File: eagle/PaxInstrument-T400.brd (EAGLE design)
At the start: 96.5 x 50.8 mm, 121 parts, among them IC1 MCP3424, U1 MCP9800, U3 MCP73831, U4 MIC5219-3.3V, U7 USD-SOCKETNEW, U8 NC7S32, X2 FH12-12S-0.5SH, Y1 RESONATORSMD

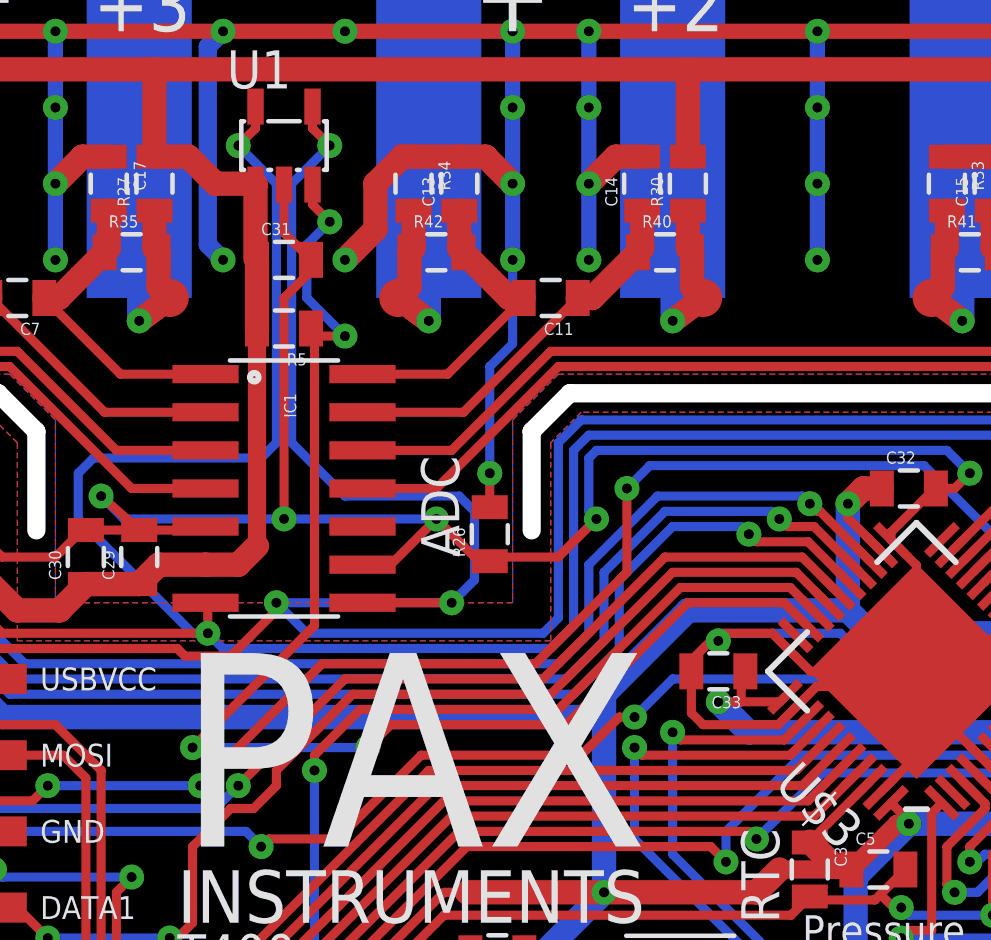
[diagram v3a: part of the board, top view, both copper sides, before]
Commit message: - Removed TEMP_INT
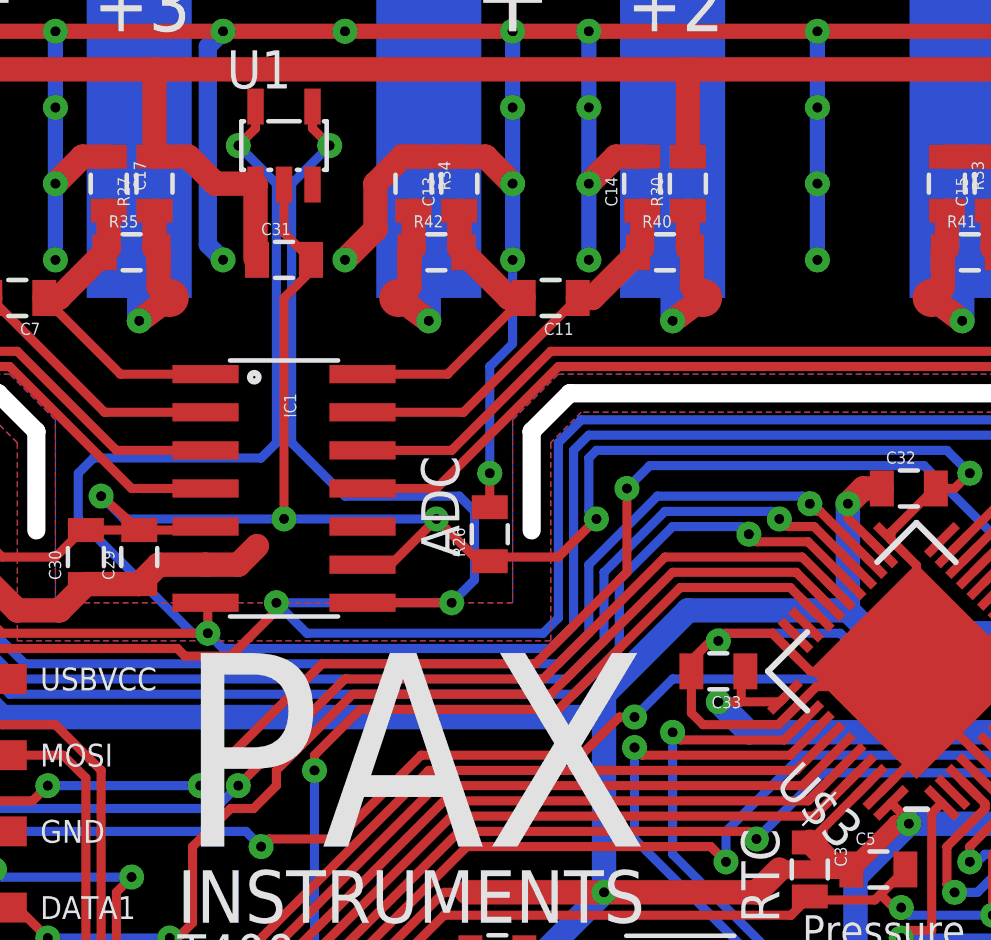
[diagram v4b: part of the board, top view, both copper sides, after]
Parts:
- removed R5: 10k, SparkFun-Passives:0805
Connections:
- removed net TEMP_INT: R5.1, U$3.31, U1.3
- new net DATA3: U$3.31
- net 3.3V: no longer R5.2
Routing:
- net TEMP_INT: track 45.8 -> 0.00 mm, vias 4 -> 0
- net 3.3V: track 365.2 -> 355.7 mm
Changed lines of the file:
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@@
 <attribute name="OC_DIGIKEY" value="N/A" x="57.15" y="44.45" size="1.778" layer="28" rot="MR180" display="off"/>
-</element>
-<element name="R5" library="SparkFun-Passives" package="0805" value="10k" x="48.26" y="38.354" rot="R180">
-<attribute name="OC_DIGIKEY" value="1276-5086-2-ND" x="48.26" y="38.354" size="1.778" layer="27" font="vector" ratio="15" rot="R180" display="off"/>
 </element>
 <element name="Z1" library="freetronics-master-v1.1" package="0603" value="PGB1010603" x="90.17" y="29.972" rot="R180">
@@
 <contactref element="U$3" pad="14"/>
 <contactref element="U$3" pad="34"/>
-<contactref element="R5" pad="2"/>
 <contactref element="U$14" pad="2"/>
 <contactref element="R16" pad="1"/>
@@
 <wire x1="45.6438" y1="30.48" x2="46.736" y2="30.48" width="0.8128" layer="1"/>
 <wire x1="46.736" y1="30.48" x2="47.36" y2="31.104" width="0.8128" layer="1"/>
-<wire x1="47.36" y1="31.104" x2="47.36" y2="38.354" width="0.6096" layer="1"/>
-<wire x1="47.36" y1="38.354" x2="47.36" y2="40.64" width="0.8128" layer="1"/>
 <wire x1="47.36" y1="40.64" x2="47.31" y2="40.69" width="0.6096" layer="1"/>
 <wire x1="47.31" y1="40.69" x2="47.31" y2="43.15" width="0.8128" layer="1"/>
@@
 <wire x1="28.702" y1="31.242" x2="29.464" y2="30.48" width="0.8128" layer="1"/>
 <contactref element="X2" pad="1"/>
-<wire x1="49.01" y1="12.61" x2="45.51" y2="12.61" width="0" layer="19" extent="1-1"/>
+<wire x1="47.36" y1="31.104" x2="47.36" y2="40.64" width="0" layer="19" extent="1-1"/>
+<wire x1="45.51" y1="12.61" x2="49.01" y2="12.61" width="0" layer="19" extent="1-1"/>
 </signal>
 <signal name="3V3EN">
@@
 <wire x1="49.276" y1="24.13" x2="49.276" y2="23.622" width="0.3048" layer="1"/>
 </signal>
-<signal name="TEMP_INT">
-<contactref element="U1" pad="3"/>
-<contactref element="R5" pad="1"/>
-<contactref element="U$3" pad="31"/>
-<wire x1="65.66504375" y1="28.479634375" x2="64.934678125" y2="29.21" width="0.3048" layer="1"/>
-<wire x1="64.934678125" y1="29.21" x2="61.722" y2="29.21" width="0.3048" layer="1"/>
-<wire x1="61.722" y1="29.21" x2="57.658" y2="25.146" width="0.3048" layer="1"/>
-<wire x1="57.658" y1="25.146" x2="51.816" y2="25.146" width="0.3048" layer="1"/>
-<wire x1="49.276" y1="28.448" x2="49.276" y2="37.962" width="0.3048" layer="1"/>
-<wire x1="49.276" y1="37.962" x2="49.16" y2="38.354" width="0.3048" layer="1"/>
-<wire x1="49.21" y1="43.15" x2="49.21" y2="42.484" width="0.3048" layer="1"/>
-<wire x1="49.21" y1="42.484" x2="49.784" y2="41.91" width="0.3048" layer="1"/>
-<via x="49.784" y="41.91" extent="1-16" drill="0.3302"/>
-<wire x1="49.784" y1="41.91" x2="49.022" y2="41.148" width="0.3048" layer="16"/>
-<wire x1="49.022" y1="41.148" x2="49.022" y2="39.37" width="0.3048" layer="16"/>
-<wire x1="49.022" y1="39.37" x2="50.292" y2="38.1" width="0.3048" layer="16"/>
-<via x="50.292" y="38.1" extent="1-16" drill="0.3302"/>
-<wire x1="50.292" y1="38.1" x2="49.414" y2="38.1" width="0.3048" layer="1"/>
-<wire x1="49.414" y1="38.1" x2="49.16" y2="38.354" width="0.3048" layer="1"/>
-<wire x1="49.276" y1="28.448" x2="45.212" y2="24.384" width="0.3048" layer="1"/>
-<via x="45.212" y="24.384" extent="1-16" drill="0.3302"/>
-<wire x1="45.212" y1="24.384" x2="51.054" y2="24.384" width="0.3048" layer="16"/>
-<via x="51.054" y="24.384" extent="1-16" drill="0.3302"/>
-<wire x1="51.054" y1="24.384" x2="51.816" y2="25.146" width="0.3048" layer="1"/>
-</signal>
 <signal name="N$18">
 </signal>
@@
 <wire x1="43.688" y1="14.086" x2="46.01" y2="12.61" width="0" layer="19" extent="1-1"/>
 </signal>
+<signal name="DATA3">
+<contactref element="U$3" pad="31"/>
+</signal>
 </signals>

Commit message: - Updated part numbers. There may be some 0804 parts sourced at 0603. Fix this.
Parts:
- R10, R9: value 22 -> 22R
- R19: value 53 -> 53R

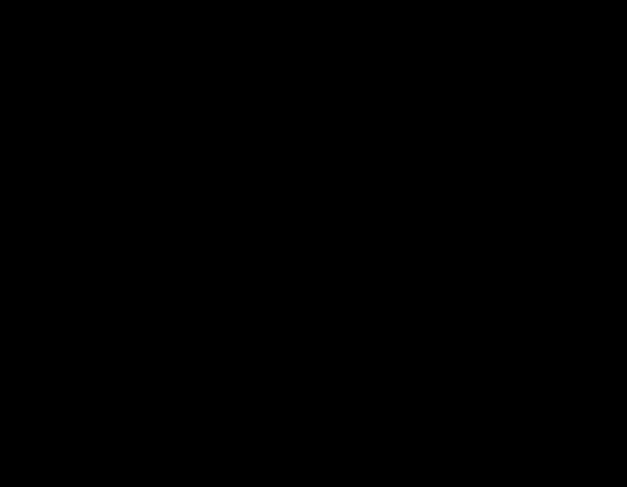
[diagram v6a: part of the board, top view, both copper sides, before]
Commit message: - Added PSI flash datasheet - Added SPI flash to charlespax library - Added SPI flash to T400 schematic - updated .gitignore
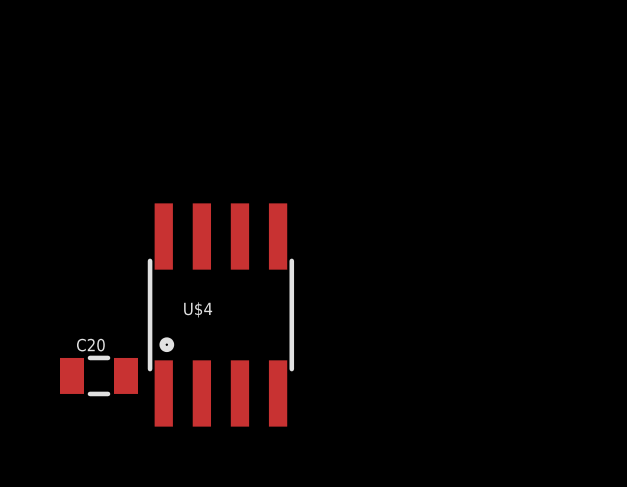
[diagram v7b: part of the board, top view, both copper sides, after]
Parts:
- added C20: 0.1uF, SparkFun-Passives:0805
- added U$4: W25Q80BV, charlespax:SOIC8
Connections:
- new net FLASH_CS: U$4.1
- net 3.3V: now also C20.2, U$4.2, U$4.3, U$4.8
- net GND: now also C20.1, U$4.7
- net MISO: now also U$4.6
- net MOSI: now also U$4.5
- net SCK: now also U$4.4
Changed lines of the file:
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@@
 <attribute name="OC_DIGIKEY" value="3000KTR-ND" x="6.35" y="34.29" size="1.778" layer="27" rot="R90" display="off"/>
+</element>
+<element name="U$4" library="charlespax" package="SOIC8" value="W25Q80BV" x="-43.688" y="-23.368"/>
+<element name="C20" library="SparkFun-Passives" package="0805" value="0.1uF" x="-47.752" y="-25.4">
+<attribute name="MPN" value="CL10B104KO8NNNC" x="-47.752" y="-25.4" size="1.778" layer="27" display="off"/>
+<attribute name="OC_DIGIKEY" value="1276-1005-2-ND" x="-47.752" y="-25.4" size="1.778" layer="27" display="off"/>
 </element>
 </elements>
@@
 <wire x1="28.702" y1="31.242" x2="29.464" y2="30.48" width="0.8128" layer="1"/>
 <contactref element="X2" pad="1"/>
-<wire x1="47.36" y1="31.104" x2="47.36" y2="40.64" width="0" layer="19" extent="1-1"/>
+<contactref element="U$4" pad="2"/>
+<contactref element="U$4" pad="8"/>
+<contactref element="C20" pad="2"/>
+<contactref element="U$4" pad="3"/>
+<wire x1="-44.323" y1="-25.9842" x2="-46.852" y2="-25.4" width="0" layer="19" extent="1-1"/>
+<wire x1="-43.053" y1="-25.9842" x2="-44.323" y2="-25.9842" width="0" layer="19" extent="1-1"/>
+<wire x1="-45.593" y1="-20.7518" x2="-46.852" y2="-25.4" width="0" layer="19" extent="1-1"/>
+<wire x1="3.048" y1="17.526" x2="-45.593" y2="-20.7518" width="0" layer="19" extent="1-1"/>
 <wire x1="45.51" y1="12.61" x2="49.01" y2="12.61" width="0" layer="19" extent="1-1"/>
+<wire x1="47.36" y1="40.64" x2="47.36" y2="31.104" width="0" layer="19" extent="1-1"/>
 </signal>
 <signal name="3V3EN">
@@
 <wire x1="17.018" y1="27.432" x2="18.542" y2="28.956" width="0.3048" layer="1"/>
 <wire x1="18.542" y1="28.956" x2="18.542" y2="31.242" width="0.3048" layer="1"/>
-<wire x1="65.162" y1="18.796" x2="62.23" y2="14.732" width="0" layer="19" extent="1-1"/>
-<wire x1="46.01" y1="14.442" x2="46.01" y2="11.466" width="0" layer="19" extent="1-1"/>
+<contactref element="U$4" pad="7"/>
+<contactref element="C20" pad="1"/>
+<wire x1="-44.323" y1="-20.7518" x2="-48.652" y2="-25.4" width="0" layer="19" extent="1-1"/>
+<wire x1="1.198" y1="9.26" x2="-44.323" y2="-20.7518" width="0" layer="19" extent="1-1"/>
+<wire x1="46.01" y1="11.466" x2="46.01" y2="14.442" width="0" layer="19" extent="1-1"/>
+<wire x1="62.23" y1="14.732" x2="65.162" y2="18.796" width="0" layer="19" extent="1-1"/>
 </signal>
 <signal name="USBVCC">
@@
 <wire x1="18.034" y1="22.352" x2="18.034" y2="25.654" width="0.4064" layer="16"/>
 <wire x1="18.034" y1="25.654" x2="17.018" y2="26.67" width="0.4064" layer="16"/>
+<contactref element="U$4" pad="6"/>
+<wire x1="5.048" y1="20.52" x2="-43.053" y2="-20.7518" width="0" layer="19" extent="1-1"/>
 </signal>
 <signal name="MOSI">
@@
 <wire x1="74.93" y1="24.638" x2="74.422" y2="24.13" width="0.3048" layer="16"/>
 <wire x1="74.422" y1="24.13" x2="65.532" y2="24.13" width="0.3048" layer="16"/>
+<contactref element="U$4" pad="5"/>
+<wire x1="5.048" y1="16.12" x2="-41.783" y2="-20.7518" width="0" layer="19" extent="1-1"/>
 </signal>
 <signal name="SCK">
@@
 <wire x1="66.211659375" y1="23.539659375" x2="75.012340625" y2="23.539659375" width="0.3048" layer="16"/>
 <wire x1="75.012340625" y1="23.539659375" x2="75.184" y2="23.622" width="0.3048" layer="16"/>
+<contactref element="U$4" pad="4"/>
+<wire x1="5.048" y1="18.32" x2="-41.783" y2="-25.9842" width="0" layer="19" extent="1-1"/>
 </signal>
 <signal name="RTC_BATT">
@@
 <contactref element="U$3" pad="31"/>
 </signal>
+<signal name="FLASH_CS">
+<contactref element="U$4" pad="1"/>
+</signal>
 </signals>

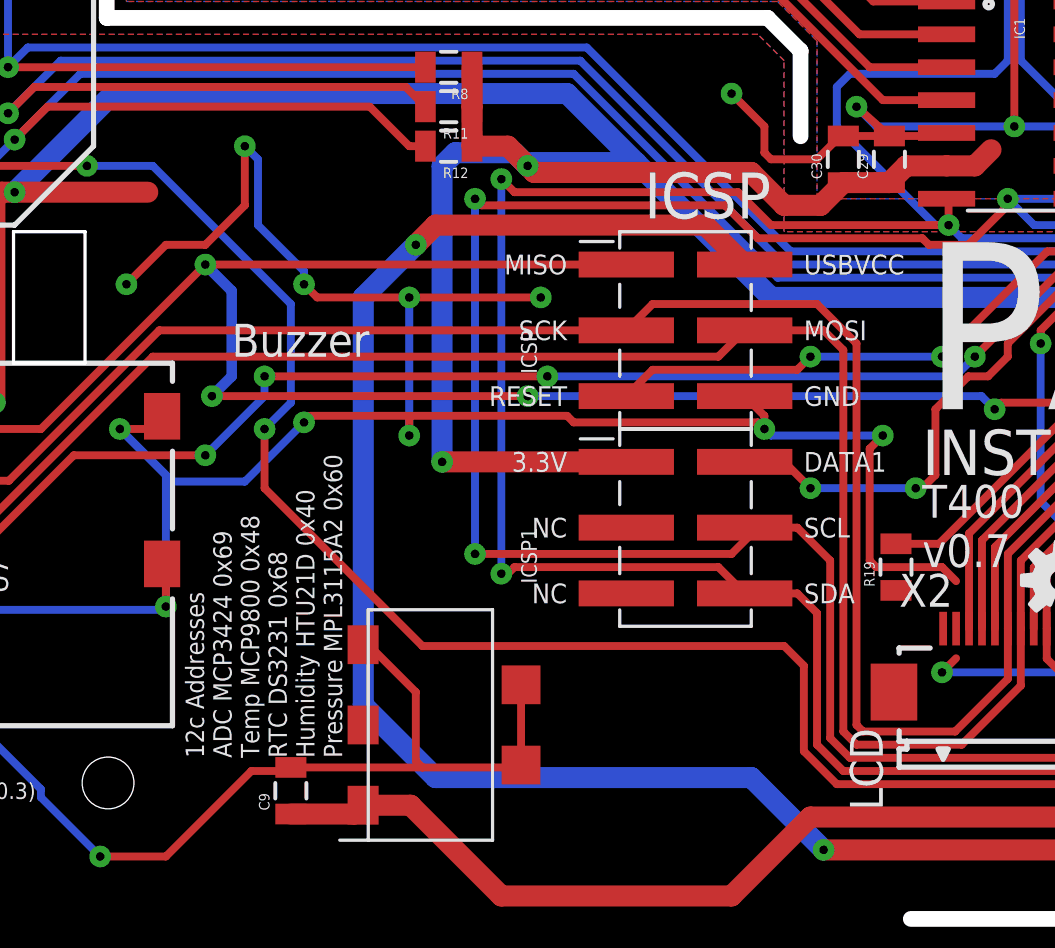
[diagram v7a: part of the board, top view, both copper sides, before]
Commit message: - Moved headers apart https://github.com/PaxInstruments/t400-electronics/issues/75
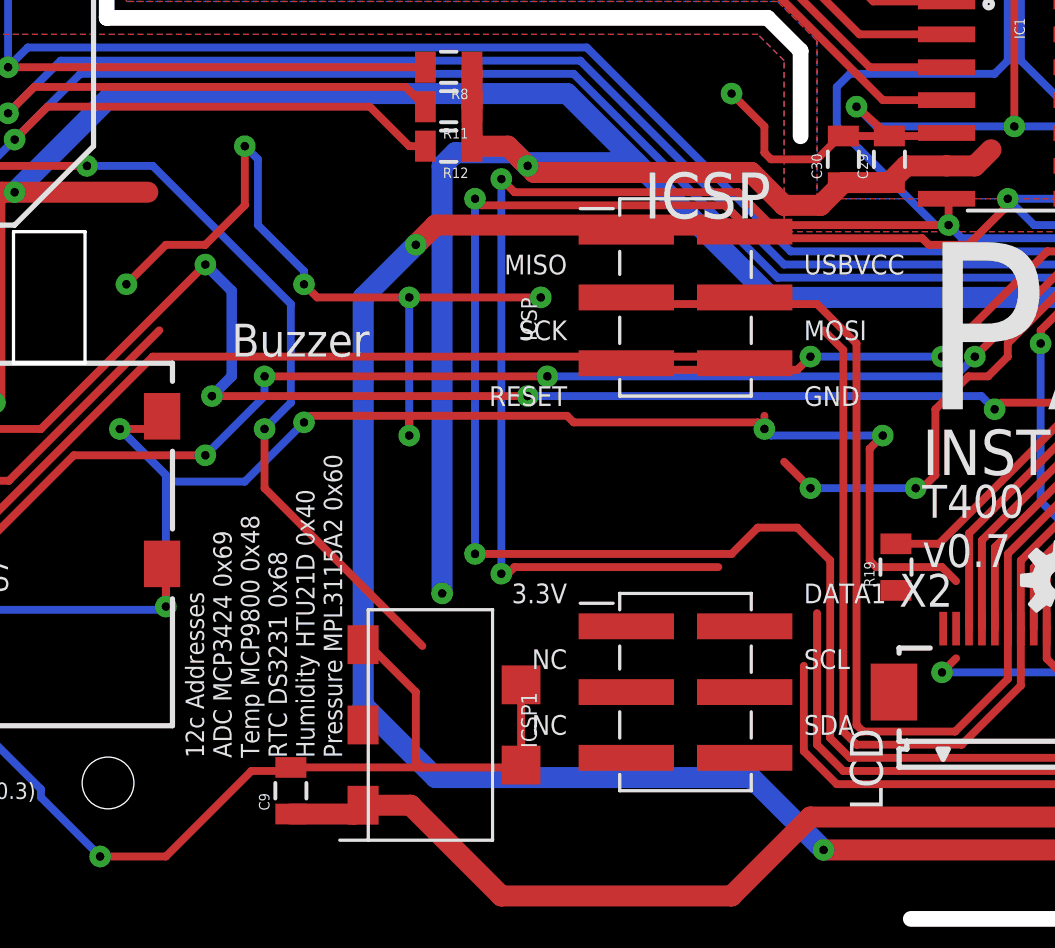
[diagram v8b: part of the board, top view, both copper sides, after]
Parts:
- moved ICSP1 6.35 mm to (35.6, 10.2)
- moved ICSP 1.27 mm to (35.6, 25.4)
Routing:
- net SCK: track 100.5 -> 82.1 mm
- net MISO: track 105.2 -> 89.0 mm
- net RTC_BATT: track 85.5 -> 70.4 mm
- net SDA: track 159.2 -> 154.7 mm
- net MOSI: track 101.1 -> 96.7 mm
- net 3.3V: track 355.7 -> 353.7 mm
- net DATA1: track 36.2 -> 34.7 mm
- net GND: track 503.8 -> 502.7 mm
- net USBVCC: track 120.1 -> 119.5 mm
- net SCL: track 170.9 -> 170.4 mm
